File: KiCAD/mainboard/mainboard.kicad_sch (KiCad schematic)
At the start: 0 parts

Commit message: schematic chagnesS
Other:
- sheet Power_Input&Generation ports: added FE_PROJ_ON, INTZ, P1P2V_BOOT, P1P2V_SW, P1P8V_BOOT, P1P8V_SW, P3P3V_BOOT, P3P3V_SW, PROJ_ON; removed none

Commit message: schematic changes
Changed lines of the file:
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@@
 	(generator_version "10.0")
 	(paper "A3")
+	(junction
+		(at 226.06 64.77)
+		(diameter 0)
+		(color 0 0 0 0)
+	)
 	(wire
 		(pts
@@
 	(wire
 		(pts
+			(xy 226.06 58.42) (xy 226.06 64.77)
+		)
+		(stroke
+			(width 0)
+			(type default)
+		)
+	)
+	(wire
+		(pts
 			(xy 85.09 69.85) (xy 91.44 69.85)
 		)
@@
 	(wire
 		(pts
+			(xy 226.06 64.77) (xy 228.6 64.77)
+		)
+		(stroke
+			(width 0)
+			(type default)
+		)
+	)
+	(wire
+		(pts
 			(xy 223.52 68.58) (xy 228.6 68.58)
 		)
@@
 	(wire
 		(pts
-			(xy 223.52 64.77) (xy 228.6 64.77)
+			(xy 223.52 64.77) (xy 226.06 64.77)
 		)
 		(stroke
@@
 	(sheet
 		(at 179.705 20.32)
-		(size 101.6 37.465)
+		(size 101.6 38.1)
 		(exclude_from_sim no)
 		(in_bom yes)
@@
 		)
 		(property "Sheetfile" "power_input&generation.kicad_sch"
-			(at 179.705 58.3696 0)
+			(at 179.705 59.0046 0)
 			(show_name no)
 			(do_not_autoplace no)
@@
 		)
 		(pin "FE_PROJ_ON" input
-			(at 190.4366 57.785 270)
+			(at 179.705 34.29 180)
 			(effects
 				(font
@@
 		)
 		(pin "INTZ" input
-			(at 225.9966 57.785 270)
+			(at 225.9966 58.42 270)
 			(effects
 				(font
@@
 		)
 		(pin "P1P2V_BOOT" input
-			(at 213.2966 57.785 270)
+			(at 179.705 43.18 180)
 			(effects
 				(font
@@
 		)
 		(pin "P1P2V_SW" input
-			(at 233.6166 57.785 270)
+			(at 179.705 46.99 180)
 			(effects
 				(font
@@
 		)
 		(pin "P1P8V_BOOT" input
-			(at 256.4766 57.785 270)
+			(at 256.4766 58.42 270)
 			(effects
 				(font
@@
 		)
 		(pin "P1P8V_SW" input
-			(at 246.3166 57.785 270)
+			(at 246.3166 58.42 270)
 			(effects
 				(font
@@
 		)
 		(pin "P3P3V_BOOT" input
-			(at 272.9866 57.785 270)
+			(at 272.9866 58.42 270)
 			(effects
 				(font
@@
 		)
 		(pin "P3P3V_SW" input
-			(at 265.3666 57.785 270)
+			(at 265.3666 58.42 270)
 			(effects
 				(font
@@
 		)
 		(pin "PROJ_ON" input
-			(at 281.305 52.705 0)
-			(effects
-				(font
-					(size 1.27 1.27)
-				)
-				(justify right)
+			(at 179.705 39.37 180)
+			(effects
+				(font
+					(size 1.27 1.27)
+				)
+				(justify left)
 			)
 		)
@@
 	)
 	(sheet
-		(at 21.5266 62.865)
-		(size 63.5634 42.5449)
+		(at 66.675 62.865)
+		(size 18.415 42.5449)
 		(exclude_from_sim no)
 		(in_bom yes)
@@
 		)
 		(property "Sheetname" "FPGA_Connections"
-			(at 21.5266 59.436 0)
+			(at 66.675 59.436 0)
 			(show_name no)
 			(do_not_autoplace no)
@@
 		)
 		(property "Sheetfile" "FPGA_Connections.kicad_sch"
-			(at 21.5266 60.706 0)
+			(at 66.675 60.706 0)
 			(show_name no)
 			(do_not_autoplace no)

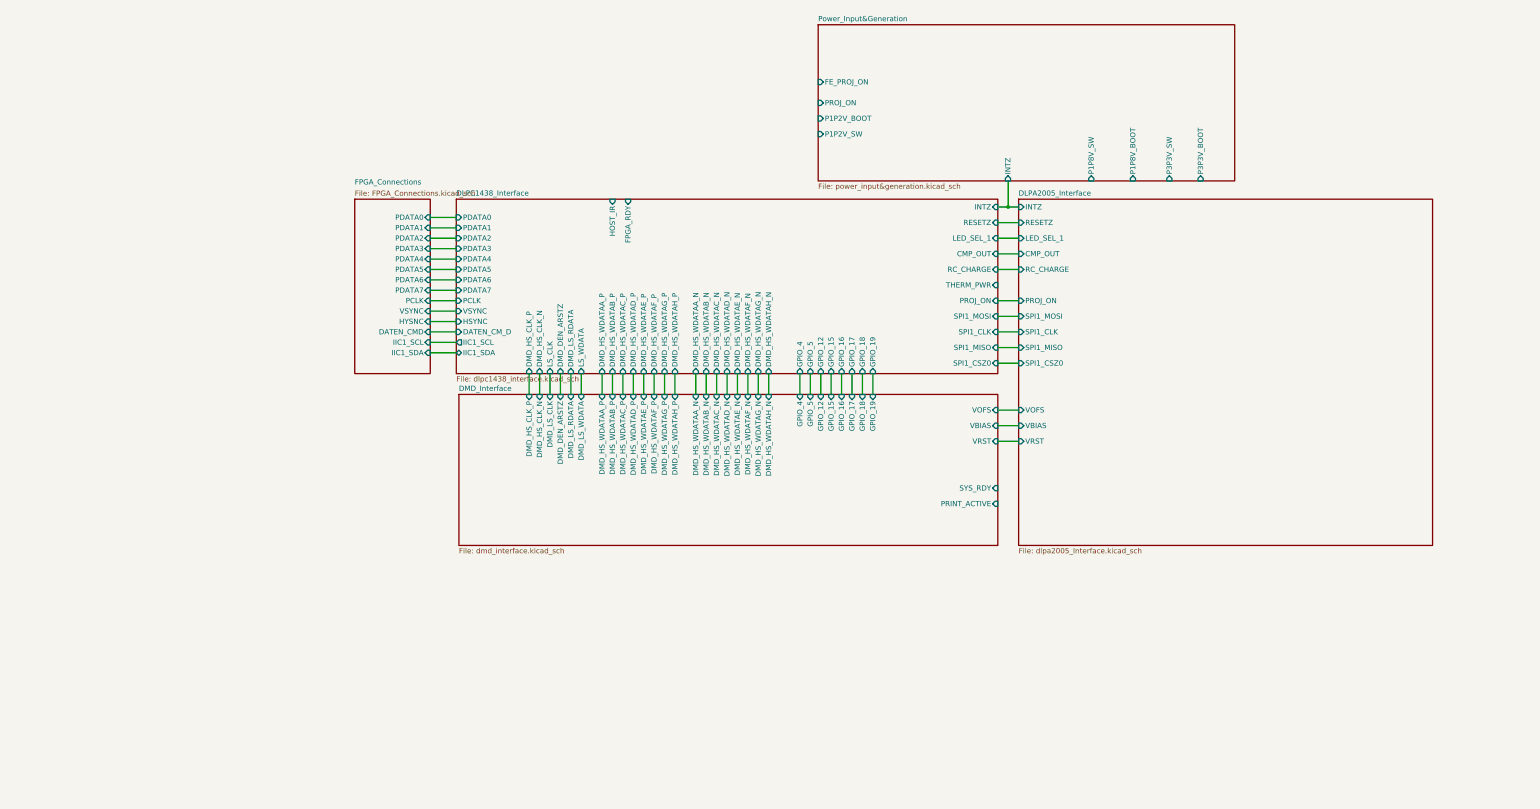
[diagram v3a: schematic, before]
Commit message: schematic changes - zero DRC errors but I have things to dicuss, and layout footprint work and rearrangment
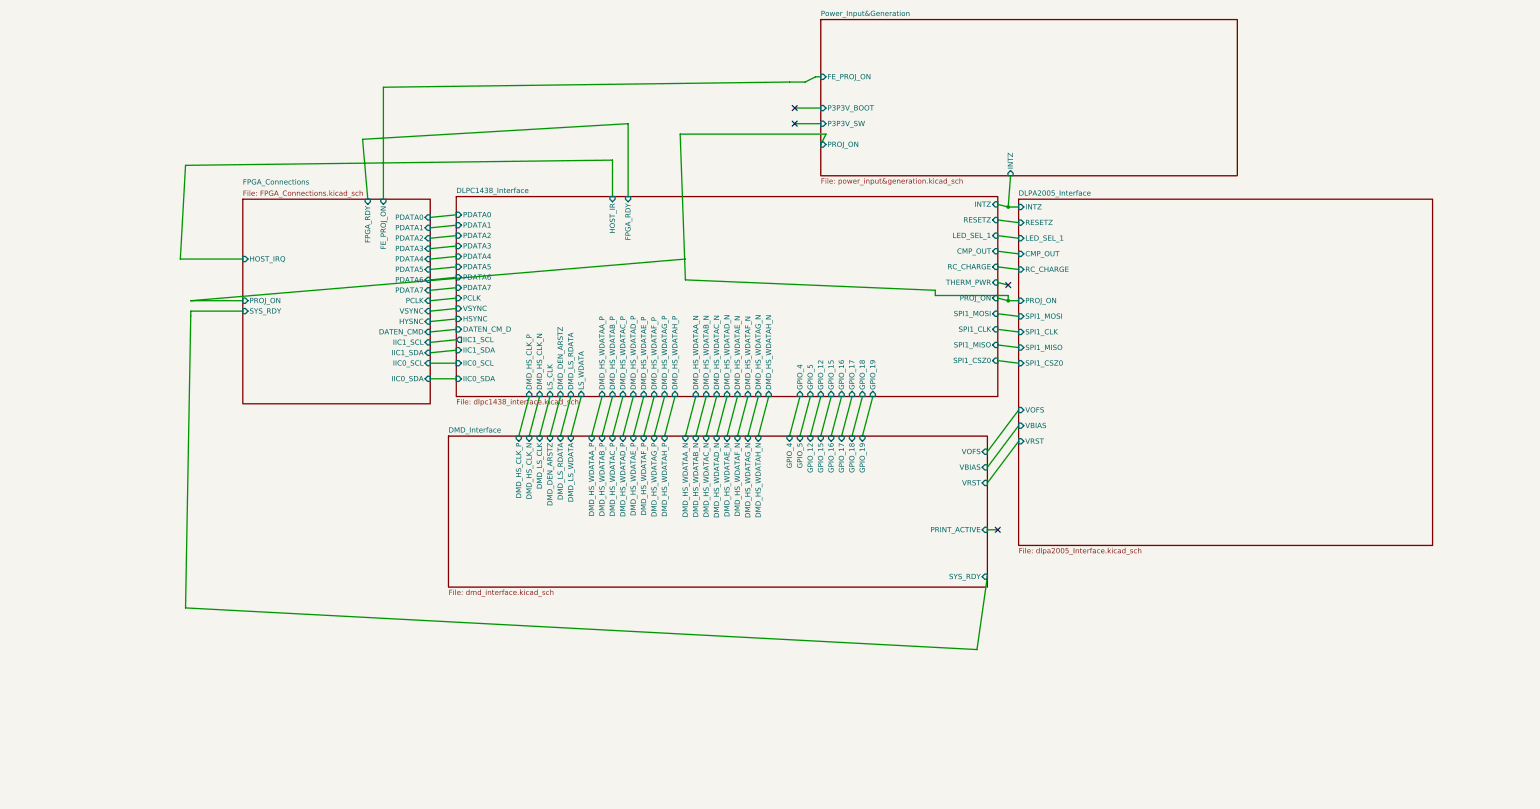
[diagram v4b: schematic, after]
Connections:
- no-connect marks 0 -> 4
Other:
- sheet DLPC1438_Interface ports: added IIC0_SCL, IIC0_SDA; removed none
- sheet FPGA_Connections ports: added FE_PROJ_ON, FPGA_RDY, HOST_IRQ, IIC0_SCL, IIC0_SDA, PROJ_ON, SYS_RDY; removed none
- sheet Power_Input&Generation ports: added none; removed P1P2V_BOOT, P1P2V_SW, P1P8V_BOOT, P1P8V_SW
